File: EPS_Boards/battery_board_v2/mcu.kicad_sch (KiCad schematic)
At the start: 15 parts, among them J2 Programming Header, J3 System Test Connector, U2 STM32F030F4Px, Y1 16 MHz

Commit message: eps: battery board: design review changes
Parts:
- removed D2: DESD3V3E1BL-7B, Resistor_SMD:R_0201_0603Metric, symbol Device:D_TVS
- U2: value STM32F030F4Px -> STM32F030F4P6
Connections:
- net BAT_INT: now reaches U2.14 (PB1)
- no-connect marks 3 -> 4
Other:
- note added: "TSSOP20 Pinout PA0: ADC0 PA1: ADC1 PA2: ADC2 PA3: ADC3 PA4: ADC4 PA5: ADC5 PA6: ADC6 PA7: ADC7 PA8: Not Available PA9: I2C_SCL / I2C_SCK? PA10: I2C_SDA PA11: PA12: PA13: SWDIO PA14: SWCLK"
- note removed: "Pin 2 - SWIM NC Double check PMOD connector pinout"
- note removed: "TSSOP20 Pinout PA0: ADC0 PA1: ADC1 PA2: ADC2 PA3: ADC3 PA4: ADC4 PA5: ADC5 PA6: ADC6 PA7: ADC7 PA8: Not Available PA9: I2C_SCL / I2C_SCK? PA10: I2C_SDA PA11: PA12: PA13: SWDIO PA14: SWCLK ADD BAT_INT"
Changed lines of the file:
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@@
 (kicad_sch (version 20211123) (generator eeschema)
   (paper "USLetter")
-  (junction (at 94.615 67.945) (diameter 0) (color 0 0 0 0)
-  )
   (junction (at 99.695 49.53) (diameter 0) (color 0 0 0 0)
   )
   (junction (at 73.66 111.125) (diameter 0) (color 0 0 0 0)
-  )
-  (junction (at 111.76 45.085) (diameter 0) (color 0 0 0 0)
   )
   (junction (at 111.76 49.53) (diameter 0) (color 0 0 0 0)
@@
   (no_connect (at 215.9 90.805))
   (no_connect (at 215.9 98.425))
+  (no_connect (at 124.46 99.695))
   (wire (pts (xy 114.3 40.005) (xy 114.3 49.53))
     (stroke (width 0) (type default) (color 0 0 0 0))
@@
     (stroke (width 0) (type default) (color 0 0 0 0))
   )
-  (wire (pts (xy 78.74 67.945) (xy 94.615 67.945))
-    (stroke (width 0) (type default) (color 0 0 0 0))
-  )
   (polyline (pts (xy 193.675 33.655) (xy 193.675 69.85))
     (stroke (width 0) (type default) (color 0 0 0 0))
@@
     (stroke (width 0) (type default) (color 0 0 0 0))
   )
-  (wire (pts (xy 78.74 59.69) (xy 78.74 67.945))
-    (stroke (width 0) (type default) (color 0 0 0 0))
-  )
   (wire (pts (xy 73.66 121.285) (xy 61.595 121.285))
     (stroke (width 0) (type default) (color 0 0 0 0))
@@
     (stroke (width 0) (type default) (color 0 0 0 0))
   )
-  (wire (pts (xy 78.74 45.085) (xy 78.74 52.07))
-    (stroke (width 0) (type default) (color 0 0 0 0))
-  )
   (wire (pts (xy 118.745 49.53) (xy 114.3 49.53))
     (stroke (width 0) (type default) (color 0 0 0 0))
@@
     (stroke (width 0) (type default) (color 0 0 0 0))
   )
-  (wire (pts (xy 94.615 67.945) (xy 94.615 71.12))
-    (stroke (width 0) (type default) (color 0 0 0 0))
-  )
   (wire (pts (xy 82.55 86.995) (xy 99.06 86.995))
     (stroke (width 0) (type default) (color 0 0 0 0))
   )
-  (wire (pts (xy 111.76 45.085) (xy 111.76 49.53))
-    (stroke (width 0) (type default) (color 0 0 0 0))
-  )
   (wire (pts (xy 89.535 49.53) (xy 89.535 52.07))
     (stroke (width 0) (type default) (color 0 0 0 0))
@@
     (stroke (width 0) (type default) (color 0 0 0 0))
   )
-  (wire (pts (xy 111.76 40.005) (xy 111.76 45.085))
+  (wire (pts (xy 111.76 40.005) (xy 111.76 49.53))
     (stroke (width 0) (type default) (color 0 0 0 0))
   )
@@
     (stroke (width 0) (type default) (color 0 0 0 0))
   )
-  (wire (pts (xy 111.76 45.085) (xy 78.74 45.085))
-    (stroke (width 0) (type default) (color 0 0 0 0))
-  )
   (wire (pts (xy 141.605 49.53) (xy 146.685 49.53))
     (stroke (width 0) (type default) (color 0 0 0 0))
@@
     (stroke (width 0) (type default) (color 0 0 0 0))
   )
-  (wire (pts (xy 94.615 61.595) (xy 94.615 67.945))
+  (wire (pts (xy 94.615 61.595) (xy 94.615 71.12))
     (stroke (width 0) (type default) (color 0 0 0 0))
   )
@@
     (effects (font (size 1.27 1.27)) (justify left bottom))
   )
-  (text "Pin 2 - SWIM NC\nDouble check PMOD connector pinout"
-    (at 200.66 107.95 0)
-    (effects (font (size 1.27 1.27)) (justify left bottom))
-  )
   (text "Decoupling Capacitors" (at 118.11 67.945 0)
     (effects (font (size 1.27 1.27)) (justify left bottom))
   )
-  (text "TSSOP20 Pinout\nPA0:  ADC0\nPA1:  ADC1\nPA2:  ADC2\nPA3:  ADC3\nPA4:  ADC4\nPA5:  ADC5\nPA6:  ADC6\nPA7:  ADC7\nPA8:  Not Available\nPA9:  I2C_SCL / I2C_SCK?\nPA10: I2C_SDA\nPA11: \nPA12: \nPA13: SWDIO\nPA14: SWCLK\n\nADD BAT_INT"
+  (text "TSSOP20 Pinout\nPA0:  ADC0\nPA1:  ADC1\nPA2:  ADC2\nPA3:  ADC3\nPA4:  ADC4\nPA5:  ADC5\nPA6:  ADC6\nPA7:  ADC7\nPA8:  Not Available\nPA9:  I2C_SCL / I2C_SCK?\nPA10: I2C_SDA\nPA11: \nPA12: \nPA13: SWDIO\nPA14: SWCLK"
     (at 151.13 122.555 0)
     (effects (font (size 1.27 1.27)) (justify left bottom))
@@
     (property "Intersheet References" "${INTERSHEET_REFS}" (id 0) (at 136.8232 91.9956 0)
       (effects (font (size 1.27 1.27)) (justify left) hide)
+    )
+  )
+  (global_label "BAT_INT" (shape input) (at 99.06 109.855 180) (fields_autoplaced)
+    (effects (font (size 1.27 1.27)) (justify right))
+    (property "Intersheet References" "${INTERSHEET_REFS}" (id 0) (at 89.5391 109.7756 0)
+      (effects (font (size 1.27 1.27)) (justify right) hide)
     )
   )
@@
     (pin "9")
   )
-  (symbol (lib_id "Device:D_TVS") (at 78.74 55.88 90) (mirror x) (unit 1)
-    (in_bom yes) (on_board yes)
-    (property "Reference" "D2" (id 0) (at 73.66 53.975 90)
-      (effects (font (size 1.27 1.27)) (justify right))
-    )
-    (property "Value" "DESD3V3E1BL-7B" (id 1) (at 59.055 57.15 90)
-      (effects (font (size 1.27 1.27)) (justify right))
-    )
-    (property "Footprint" "Resistor_SMD:R_0201_0603Metric" (id 2) (at 78.74 55.88 0)
-      (effects (font (size 1.27 1.27)) hide)
-    )
-    (property "Datasheet" "https://www.diodes.com/assets/Datasheets/DESD3V3E1BL.pdf" (id 3) (at 78.74 55.88 0)
-      (effects (font (size 1.27 1.27)) hide)
-    )
-    (pin "1")
-    (pin "2")
-  )
   (symbol (lib_id "Device:C") (at 146.685 55.245 0) (unit 1)
     (in_bom yes) (on_board yes) (fields_autoplaced)
@@
   (symbol (lib_id "MCU_ST_STM32F0:STM32F030F4Px") (at 111.76 94.615 0) (unit 1)
     (in_bom yes) (on_board yes) (fields_autoplaced)
-    (property "Reference" "U2" (id 0) (at 113.7794 115.189 0)
-      (effects (font (size 1.27 1.27)) (justify left))
-    )
-    (property "Value" "STM32F030F4Px" (id 1) (at 113.7794 117.729 0)
-      (effects (font (size 1.27 1.27)) (justify left))
-    )
+    (property "Reference" "U2" (id 0) (at 113.7794 115.57 0)
+      (effects (font (size 1.27 1.27)) (justify left))
+    )
+    (property "Value" "STM32F030F4P6" (id 1) (at 113.7794 118.11 0)
+      (effects (font (size 1.27 1.27)) (justify left))
+    )

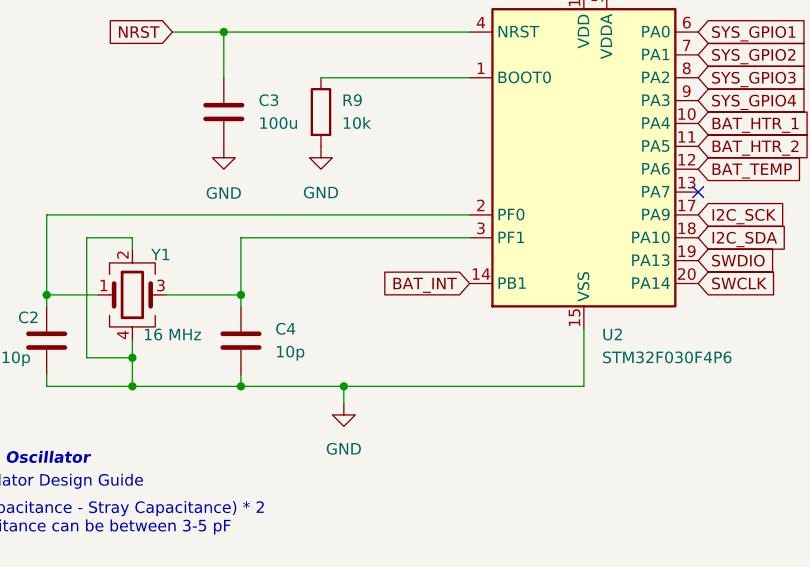
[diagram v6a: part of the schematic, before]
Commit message: eps: battery board: second design review changes
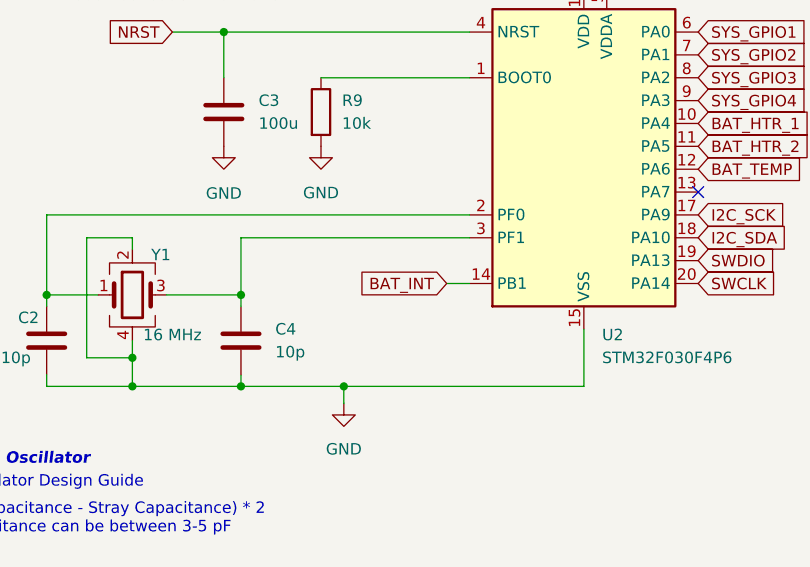
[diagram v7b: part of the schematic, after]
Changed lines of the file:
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@@
+    (stroke (width 0) (type default) (color 0 0 0 0))
+  )
+  (wire (pts (xy 96.52 109.855) (xy 99.06 109.855))
     (stroke (width 0) (type default) (color 0 0 0 0))
   )
@@
     )
   )
-  (global_label "BAT_INT" (shape input) (at 99.06 109.855 180) (fields_autoplaced)
-    (effects (font (size 1.27 1.27)) (justify right))
-    (property "Intersheet References" "${INTERSHEET_REFS}" (id 0) (at 89.5391 109.7756 0)
-      (effects (font (size 1.27 1.27)) (justify right) hide)
-    )
+  (global_label "BAT_INT" (shape input) (at 96.52 109.855 180) (fields_autoplaced)
+    (effects (font (size 1.27 1.27)) (justify right))
+    (property "Intersheet References" "${INTERSHEET_REFS}" (id 0) (at 86.9991 109.7756 0)
+      (effects (font (size 1.27 1.27)) (justify right) hide)
+    )

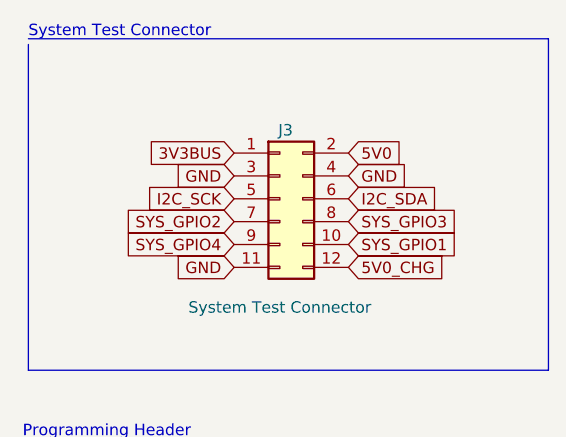
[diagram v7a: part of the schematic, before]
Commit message: eps: battery board: pre-layout review
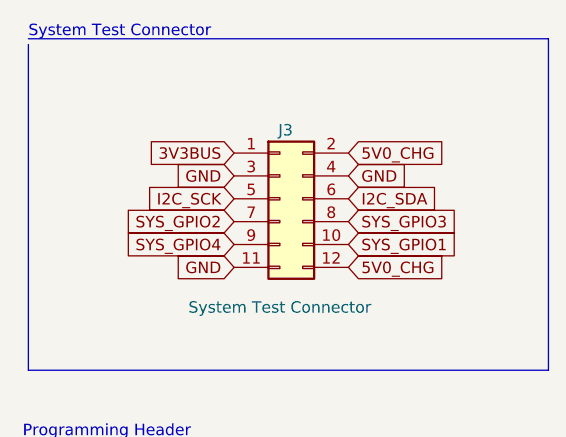
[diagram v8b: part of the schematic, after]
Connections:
- net 5V0 is gone; now on net 5V0_CHG: J3.2 (Pin_2)
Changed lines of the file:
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@@
     )
   )
-  (global_label "5V0" (shape input) (at 229.235 45.72 0) (fields_autoplaced)
+  (global_label "5V0_CHG" (shape input) (at 229.235 45.72 0) (fields_autoplaced)
     (effects (font (size 1.27 1.27)) (justify left))
-    (property "Intersheet References" "${INTERSHEET_REFS}" (id 0) (at 235.0668 45.6406 0)
+    (property "Intersheet References" "${INTERSHEET_REFS}" (id 0) (at 239.9049 45.6406 0)
       (effects (font (size 1.27 1.27)) (justify left) hide)
     )
